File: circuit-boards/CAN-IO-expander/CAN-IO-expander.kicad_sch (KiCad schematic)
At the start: 39 parts, among them J1 PROG, J2 CAN1, J3 CAN1, J4 Conn_01x06_Pin, J5 Conn_01x03_Pin, J6 Conn_01x06_Pin, J7 Conn_01x03_Pin, J8 Power, U1 RP2350_60QFN, U10 24LC01BT-I/OT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

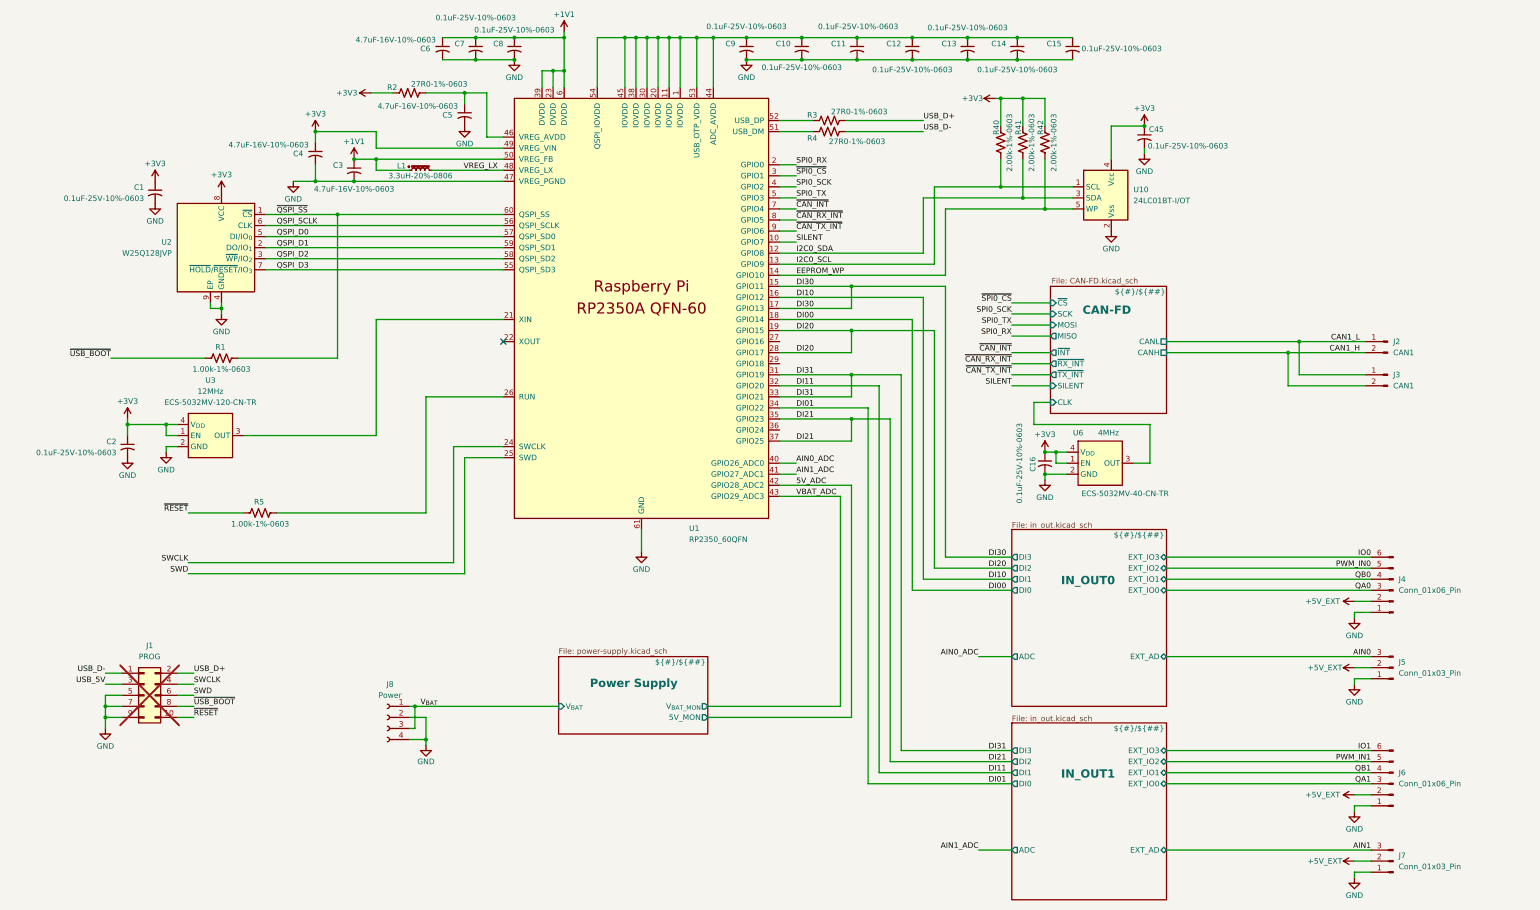
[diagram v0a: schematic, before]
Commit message: Changed to 1 encoder, all connectors to SMD right angle SL
Signed-off-by: Scott Berman <sgberman1@gmail.com>
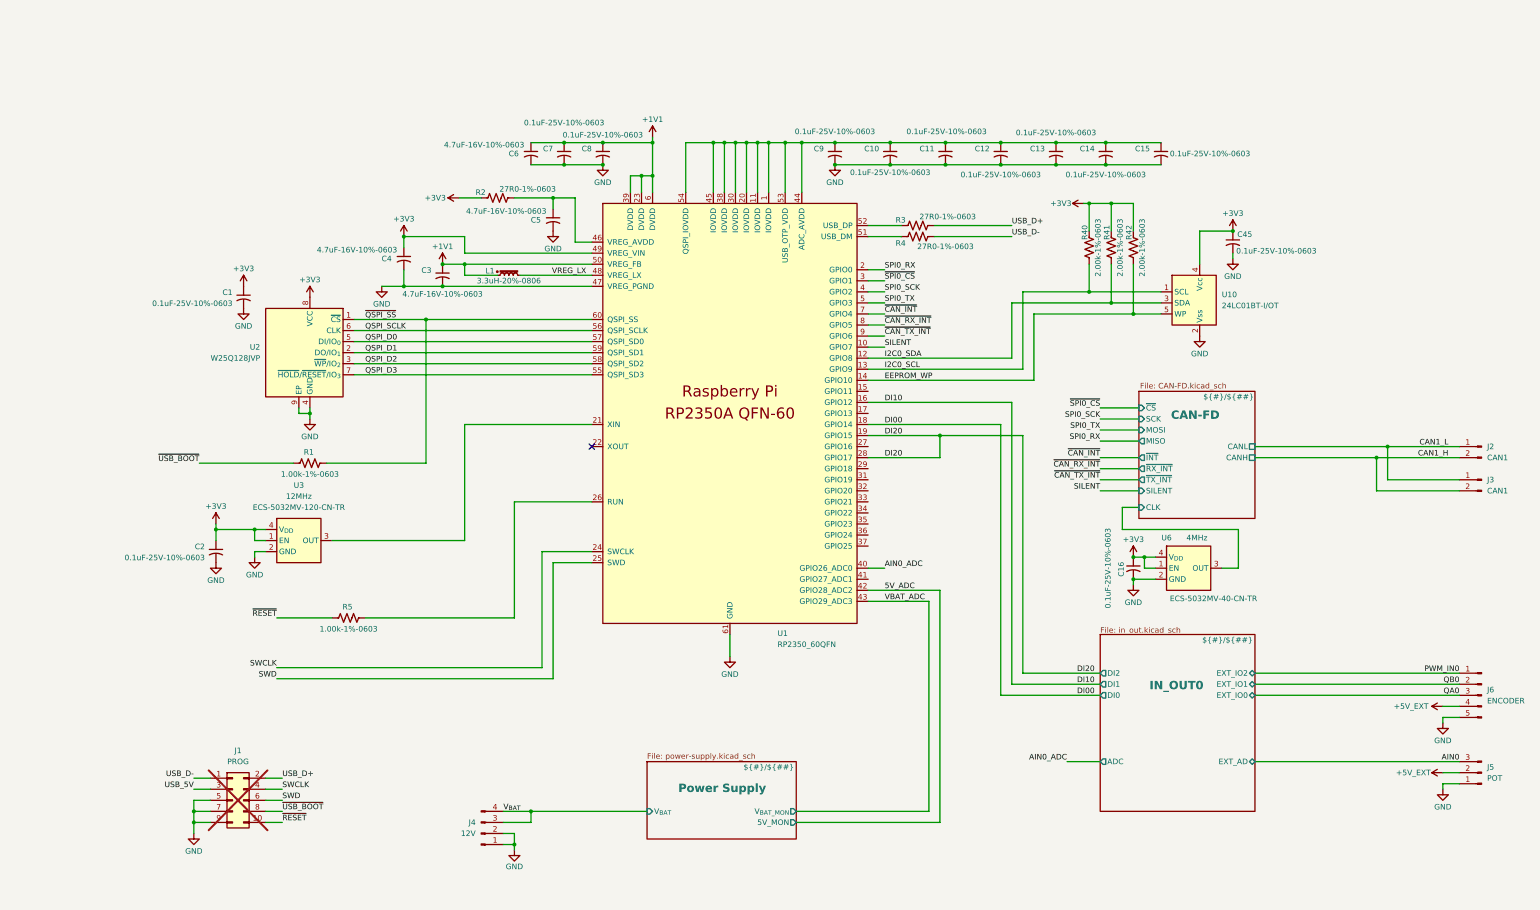
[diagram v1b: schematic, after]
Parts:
- removed J4, J6: Conn_01x06_Pin, CAN-IO-expander:70555-0005, symbol Connector:Conn_01x06_Pin
- removed J7: Conn_01x03_Pin, CAN-IO-expander:70555-0002, symbol Connector:Conn_01x03_Pin
- removed J8: Power, CAN-IO-expander:Wago-2604-3102, symbol Connector:Conn_01x04_Socket
- added J4: 12V, CAN-IO-expander:Molex-70634-0038, symbol Connector:Conn_01x04_Pin
- added J6: ENCODER, CAN-IO-expander:Molex-70634-0039, symbol Connector:Conn_01x05_Pin
- J2, J3: footprint CAN-IO-expander:70555-0001 -> CAN-IO-expander:Molex-70634-0036; DIST P/N WM4175-ND -> WM1340-ND; MFG P/N 0705550036 -> 0015912025
- J5: value Conn_01x03_Pin -> POT; footprint CAN-IO-expander:70555-0002 -> CAN-IO-expander:Molex-70634-0037; DIST (none) -> Digikey; DIST P/N (none) -> WM1341-ND; MFG (none) -> Molex; MFG P/N (none) -> 0015912035
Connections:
- net +5V_EXT: now also J6.4 (Pin_4)
- net GND: now also J4.1 (Pin_1), J4.2 (Pin_2), J6.5 (Pin_5)
- net PWM_IN0: now also J6.1 (Pin_1)
- net QA0: now also J6.3 (Pin_3)
- net QB0: now also J6.2 (Pin_2)
- net V_{BAT}: now also J4.3 (Pin_3), J4.4 (Pin_4)
- net AIN1_ADC: no longer names the net of U1.41 (GPIO27_ADC1)
- net DI01: no longer names the net of U1.34 (GPIO22)
- net DI11: no longer names the net of U1.32 (GPIO20)
- net DI21: no longer names the net of U1.35 (GPIO23)
- net DI21: no longer U1.37 (GPIO25)
- net DI30: no longer names the net of U1.15 (GPIO11)
- net DI30: no longer U1.17 (GPIO13)
- net DI31: no longer names the net of U1.31 (GPIO19)
- net DI31: no longer U1.33 (GPIO21)
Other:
- removed sheet IN_OUT1
- sheet IN_OUT0 ports: added none; removed DI3, EXT_IO3
- moved on the sheet: C1, C10, C11, C12, C13, C14, C15, C16, C2, C3, C4, C45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
